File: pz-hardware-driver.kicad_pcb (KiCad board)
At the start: 2 copper layers, 0 parts

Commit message: Added the transformer, a few LEDs, the optocoupler. All these need more work.
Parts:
- added T1: FS10-250-C2, pz-hardware-driver:FS10-250-C2, F.Cu at (112.5, 102.2)
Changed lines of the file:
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@@
     (tracks 0)
     (zones 0)
-    (modules 0)
+    (modules 1)
     (nets 1)
   )
@@
     (uvia_dia 0.3)
     (uvia_drill 0.1)
+    (add_net "Net-(T1-Pad1)")
+    (add_net "Net-(T1-Pad2)")
+    (add_net "Net-(T1-Pad3)")
+    (add_net "Net-(T1-Pad4)")
+    (add_net "Net-(T1-Pad5)")
+    (add_net "Net-(T1-Pad6)")
+    (add_net "Net-(T1-Pad7)")
+    (add_net "Net-(T1-Pad8)")
+  )
+  (module pz-hardware-driver:FS10-250-C2 (layer F.Cu)
+    (at 112.55 102.2)
+    (fp_text reference T1 (at 0 20.5) (layer F.SilkS)
+      (effects (font (size 1 1) (thickness 0.15)))
+    )
+    (fp_text value FS10-250-C2 (at 0 -17.75) (layer F.Fab)
+      (effects (font (size 1 1) (thickness 0.15)))
+    )
+    (fp_line (start -19 17.25) (end -19 -14.75) (layer F.SilkS) (width 0.2))
+    (fp_line (start -17.75 -16.75) (end 17.25 -16.75) (layer F.SilkS) (width 0.2))
+    (pad 8 thru_hole circle (at 9.5 -14.5) (size 2 2) (drill 1.25) (layers *.Cu *.Mask))
+    (pad 7 thru_hole circle (at 3 -14.5) (size 2 2) (drill 1.25) (layers *.Cu *.Mask))
+    (pad 6 thru_hole circle (at -3.5 -14.5) (size 2 2) (drill 1.25) (layers *.Cu *.Mask))
+    (pad 5 thru_hole circle (at -10 15.98) (size 2 2) (drill 1.25) (layers *.Cu *.Mask))
+    (pad 4 thru_hole circle (at 9.5 15.98) (size 2 2) (drill 1.25) (layers *.Cu *.Mask))
+    (pad 3 thru_hole circle (at 3 15.98) (size 2 2) (drill 1.25) (layers *.Cu *.Mask))
+    (pad 2 thru_hole circle (at -3.5 15.98) (size 2 2) (drill 1.25) (layers *.Cu *.Mask))
+    (pad 1 thru_hole rect (at -10 -14.5) (size 2 2) (drill 1.25) (layers *.Cu *.Mask))
+    (model ${KIPRJMOD}/models/FS10-250.step
+      (at (xyz 0 0 0))
+      (scale (xyz 1 1 1))
+      (rotate (xyz 0 0 0))
+    )
   )
 )

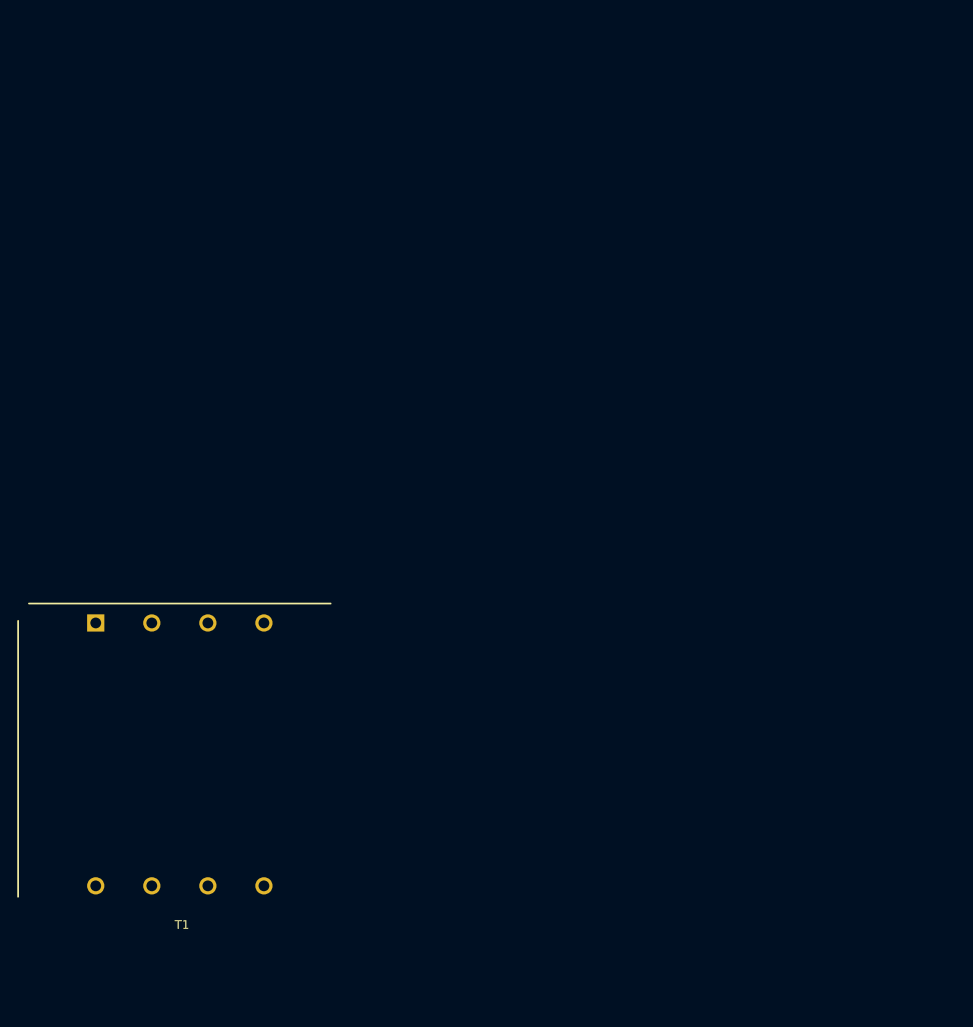
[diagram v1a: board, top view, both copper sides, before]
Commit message: Added basic parts, footprints and 3D models.
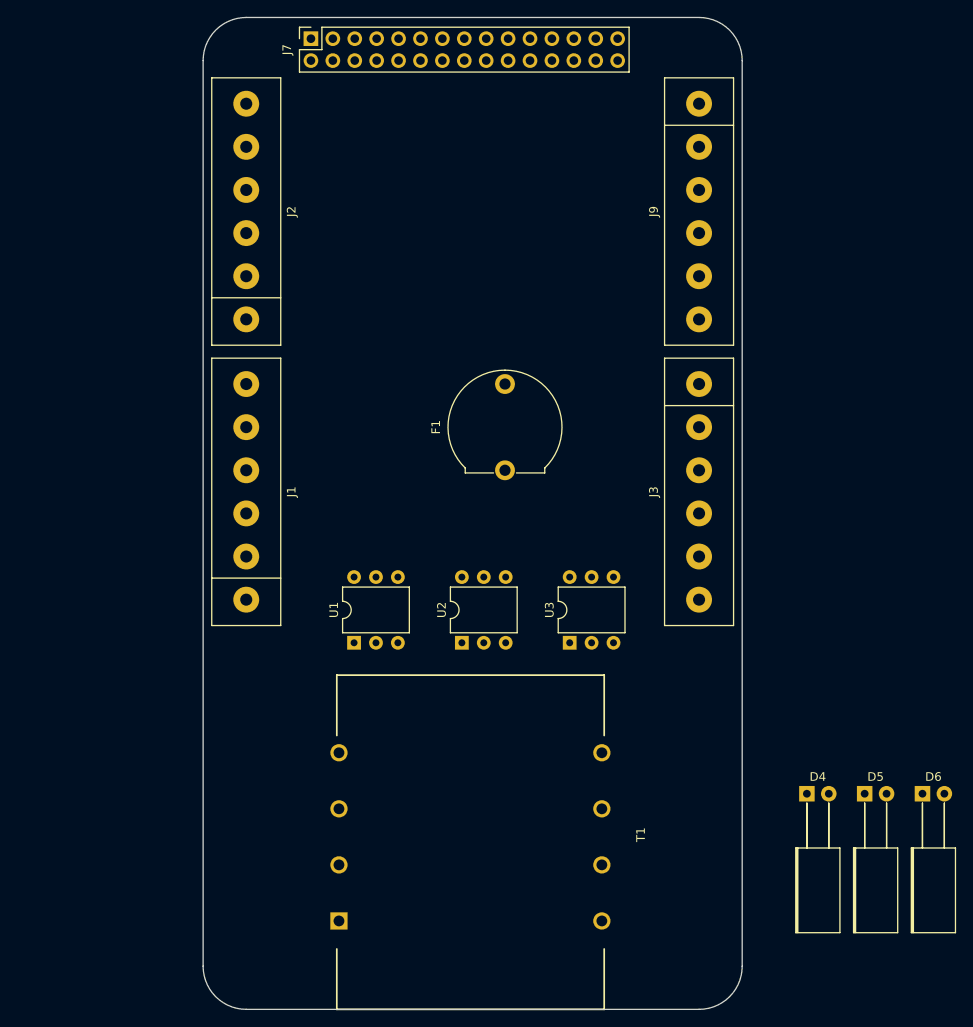
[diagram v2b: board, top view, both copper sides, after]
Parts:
- added D4: Fan LED, LED_THT:LED_Rectangular_W5.0mm_H2.0mm_Horizontal_O6.35mm_Z5.0mm, F.Cu at (185.0, 107.5)
- added D5: Rod LED, LED_THT:LED_Rectangular_W5.0mm_H2.0mm_Horizontal_O6.35mm_Z5.0mm, F.Cu at (191.7, 107.5)
- added D6: Auger LED, LED_THT:LED_Rectangular_W5.0mm_H2.0mm_Horizontal_O6.35mm_Z5.0mm, F.Cu at (198.4, 107.5)
- added F1: Fuse, Fuse:Fuseholder_Cylinder-5x20mm_EATON_H15-V-1_Vertical_Closed, F.Cu at (150.0, 70.0)
- added J1: RTD 1-2, pz-hardware-driver:TB002-500-06BE, F.Cu at (120.0, 72.5)
- added J2: RTD 3-4, pz-hardware-driver:TB002-500-06BE, F.Cu at (120.0, 40.0)
- added J3: RTD 5-6, pz-hardware-driver:TB002-500-06BE, F.Cu at (172.5, 72.5)
- added J7: Logic Header, Connector_PinSocket_2.54mm:PinSocket_2x15_P2.54mm_Vertical, F.Cu at (127.5, 20.0)
- added J9: Enhanced, pz-hardware-driver:TB002-500-06BE, F.Cu at (172.5, 40.0)
- added U1: H11L1, Package_DIP:DIP-6_W7.62mm, F.Cu at (132.5, 90.0)
- added U2: H11L1, Package_DIP:DIP-6_W7.62mm, F.Cu at (145.0, 90.0)
- added U3: H11L1, Package_DIP:DIP-6_W7.62mm, F.Cu at (157.5, 90.0)
- moved T1 34.0 mm to (145.0, 112.5), turned to 90 degrees
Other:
- board outline added: 62.5 x 115 mm
